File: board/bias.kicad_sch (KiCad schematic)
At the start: 8 parts, among them U1901 TPS65132W

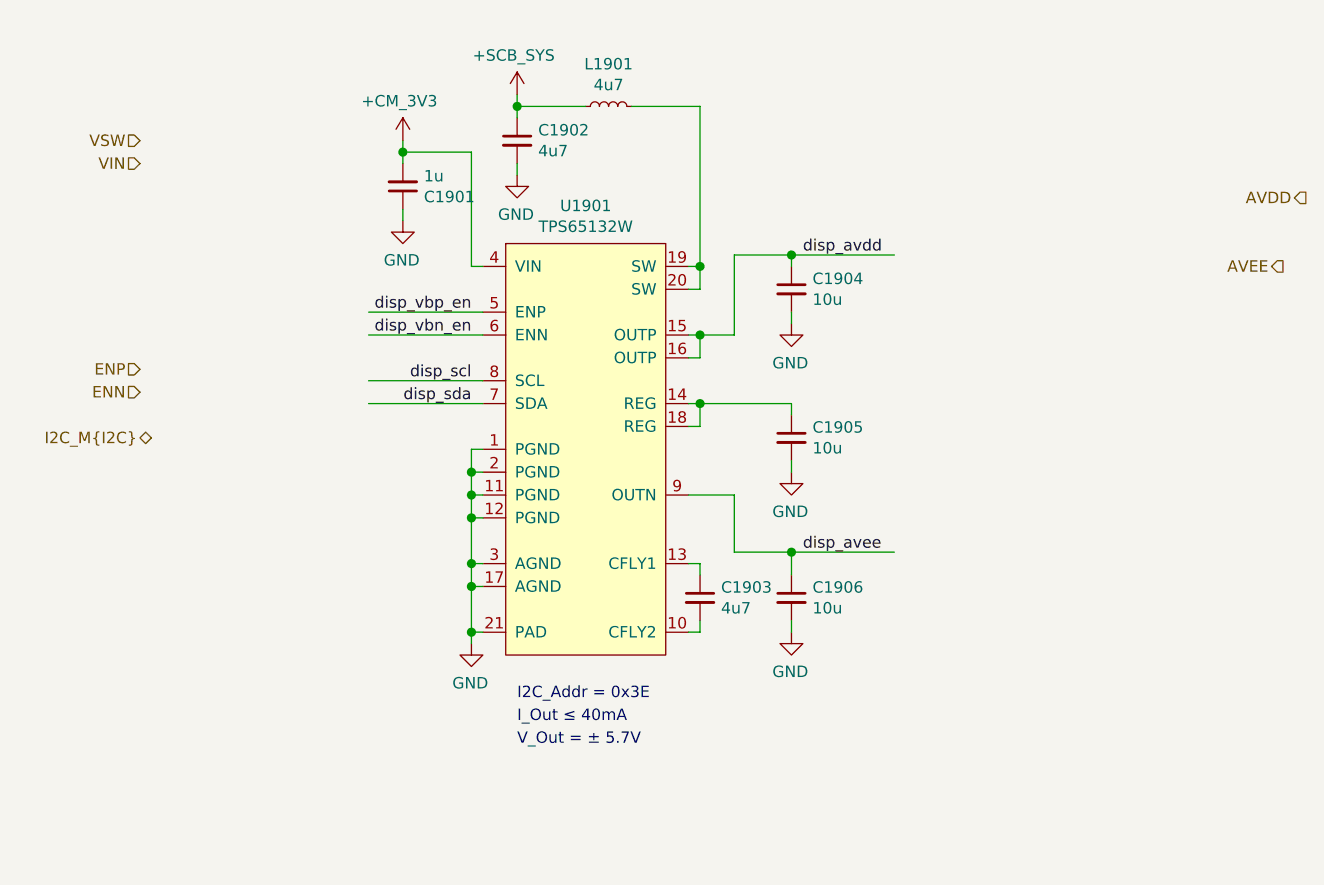
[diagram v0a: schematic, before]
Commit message: Added testpoints and other fixes
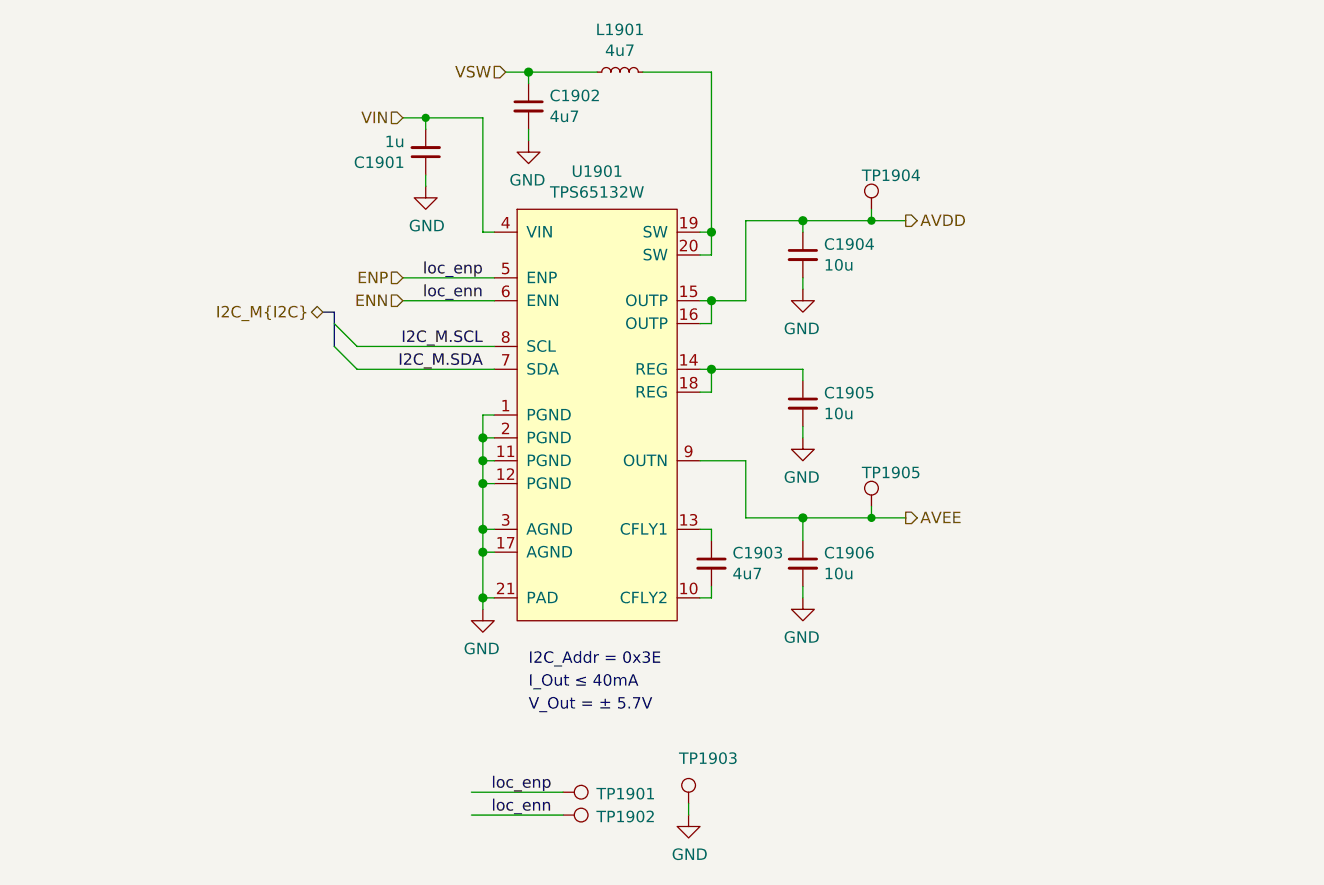
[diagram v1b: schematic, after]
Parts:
- added TP1901, TP1902, TP1903, TP1904, TP1905: TestPoint, DIYPie:TestPoint_Pad_D1.5mm, symbol DIYPie:TestPoint
- U1901: footprint DIYPie:TI_TPS65132WRVC -> Package_DFN_QFN:QFN-20-1EP_3x4mm_P0.5mm_EP1.65x2.65mm_ThermalVias
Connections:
- net +3V3 is gone; now on net VIN: C1901.2, U1901.4 (VIN)
- net +5V is gone; now on net VSW: C1902.1, L1901.1
- net disp_avdd is gone; now on net AVDD: C1904.1, U1901.15 (OUTP), U1901.16 (OUTP)
- net disp_avee is gone; now on net AVEE: C1906.1, U1901.9 (OUTN)
- net disp_vbn_en is gone; now on net ENN: U1901.6 (ENN)
- net disp_vbp_en is gone; now on net ENP: U1901.5 (ENP)
- net AVDD: now also TP1904.1
- net AVEE: now also TP1905.1
- net ENN: now also TP1902.1
- net ENP: now also TP1901.1
- net GND: now also TP1903.1
- net disp_scl renamed I2C_M.SCL
- net disp_sda renamed I2C_M.SDA
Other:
- moved on the sheet: C1901, C1902, C1903, C1904, C1905, C1906, L1901, U1901
